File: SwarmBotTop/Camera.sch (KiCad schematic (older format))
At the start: 3 parts, among them J6 Conn_01x24_Female

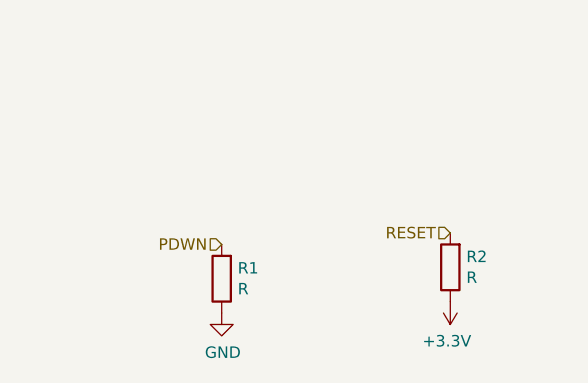
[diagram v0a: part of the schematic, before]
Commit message: Camera routing with all sensors and motors
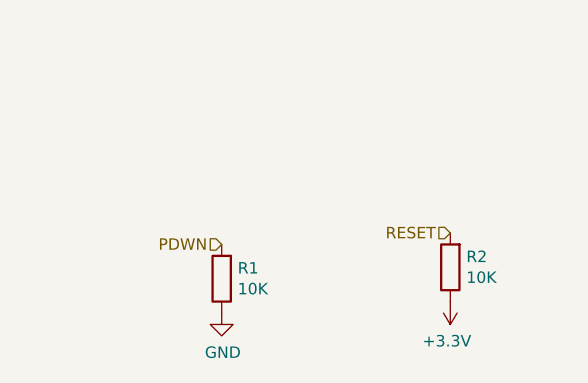
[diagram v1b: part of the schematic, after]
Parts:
- R1, R2: value R -> 10K
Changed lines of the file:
@@
 P 2250 3550
 F 0 "R1" H 2180 3504 50  0000 R CNN
-F 1 "R" H 2180 3595 50  0000 R CNN
+F 1 "10K" H 2180 3595 50  0000 R CNN
 F 2 "Resistor_SMD:R_0402_1005Metric" V 2180 3550 50  0001 C CNN
 F 3 "~" H 2250 3550 50  0001 C CNN
@@
 P 3250 3500
 F 0 "R2" H 3180 3454 50  0000 R CNN
-F 1 "R" H 3180 3545 50  0000 R CNN
+F 1 "10K" H 3180 3545 50  0000 R CNN
 F 2 "Resistor_SMD:R_0402_1005Metric" V 3180 3500 50  0001 C CNN
 F 3 "~" H 3250 3500 50  0001 C CNN

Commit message: V1 ready to order
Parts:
- removed J6: Conn_01x24_Female, Connector_FFC-FPC:Hirose_FH12-24S-0.5SH_1x24-1MP_P0.50mm_Horizontal, symbol Connector:Conn_01x24_Female
- added U9: 62674-241121ALF, ffc:FCI_62674-241121ALF, symbol 62674-241121ALF:62674-241121ALF
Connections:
- net +1V35: now also U9.15
- net +2V8: now also U9.21
- net +3V3: now also U9.14
- net GND: now also U9.10, U9.23
- net HREF: now also U9.16
- net PCKL: now also U9.8
- net PDWN: now also U9.17
- net RESET: now also U9.19
- net SCL: now also U9.20
- net SDA: now also U9.22
- net VSYNC: now also U9.18
- net XCLK: now also U9.12
- net Y2: now also U9.6
- net Y3: now also U9.4
- net Y4: now also U9.3
- net Y5: now also U9.5
- net Y6: now also U9.7
- net Y7: now also U9.9
- net Y8: now also U9.11
- net Y9: now also U9.13
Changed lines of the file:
@@
 $EndDescr
-$Comp
-L Connector:Conn_01x24_Female J6
-U 1 1 5DE89F78
-P 2550 1250
-F 0 "J6" V 2715 1180 50  0000 C CNN
-F 1 "Conn_01x24_Female" V 2624 1180 50  0000 C CNN
-F 2 "Connector_FFC-FPC:Hirose_FH12-24S-0.5SH_1x24-1MP_P0.50mm_Horizontal" H 2550 1250 50  0001 C CNN
-F 3 "~" H 2550 1250 50  0001 C CNN
-	1    2550 1250
-	0    -1   -1   0
-$EndComp
-NoConn ~ 3750 1450
-NoConn ~ 3650 1450
-NoConn ~ 1450 1450
-$Comp
-L power:GND #PWR0167
-U 1 1 5DE8C289
-P 2850 1450
-F 0 "#PWR0167" H 2850 1200 50  0001 C CNN
-F 1 "GND" H 2855 1277 50  0000 C CNN
-F 2 "" H 2850 1450 50  0001 C CNN
-F 3 "" H 2850 1450 50  0001 C CNN
-	1    2850 1450
-	1    0    0    -1
-$EndComp
-$Comp
-L power:GND #PWR0169
-U 1 1 5DE8C618
-P 1550 1450
-F 0 "#PWR0169" H 1550 1200 50  0001 C CNN
-F 1 "GND" H 1555 1277 50  0000 C CNN
-F 2 "" H 1550 1450 50  0001 C CNN
-F 3 "" H 1550 1450 50  0001 C CNN
-	1    1550 1450
-	1    0    0    -1
-$EndComp
-$Comp
-L power:+2V8 #PWR0170
-U 1 1 5DE8CB15
-P 1750 1450
-F 0 "#PWR0170" H 1750 1300 50  0001 C CNN
-F 1 "+2V8" H 1765 1623 50  0000 C CNN
-F 2 "" H 1750 1450 50  0001 C CNN
-F 3 "" H 1750 1450 50  0001 C CNN
-	1    1750 1450
-	-1   0    0    1
-$EndComp
-Text HLabel 1650 1450 3    50   Input ~ 0
-SDA
-Text HLabel 1850 1450 3    50   Input ~ 0
-SCL
-Text HLabel 1950 1450 3    50   Input ~ 0
-RESET
-Text HLabel 2050 1450 3    50   Input ~ 0
-VSYNC
-Text HLabel 2150 1450 3    50   Input ~ 0
-PDWN
-Text HLabel 2250 1450 3    50   Input ~ 0
-HREF
-$Comp
-L power:+1V35 #PWR0171
-U 1 1 5DE8D87F
-P 2350 1450
-F 0 "#PWR0171" H 2350 1300 50  0001 C CNN
-F 1 "+1V35" H 2365 1623 50  0000 C CNN
-F 2 "" H 2350 1450 50  0001 C CNN
-F 3 "" H 2350 1450 50  0001 C CNN
-	1    2350 1450
-	-1   0    0    1
-$EndComp
-$Comp
-L power:+3.3V #PWR0172
-U 1 1 5DE8DDE0
-P 2450 1450
-F 0 "#PWR0172" H 2450 1300 50  0001 C CNN
-F 1 "+3.3V" H 2465 1623 50  0000 C CNN
-F 2 "" H 2450 1450 50  0001 C CNN
-F 3 "" H 2450 1450 50  0001 C CNN
-	1    2450 1450
-	-1   0    0    1
-$EndComp
-Text HLabel 2550 1450 3    50   Input ~ 0
-Y9
-Text HLabel 2650 1450 3    50   Input ~ 0
-XCLK
-Text HLabel 2750 1450 3    50   Input ~ 0
-Y8
-Text HLabel 2950 1450 3    50   Input ~ 0
-Y7
-Text HLabel 3050 1450 3    50   Input ~ 0
-PCKL
-Text HLabel 3150 1450 3    50   Input ~ 0
-Y6
-Text HLabel 3350 1450 3    50   Input ~ 0
-Y5
-Text HLabel 3250 1450 3    50   Input ~ 0
-Y2
-Text HLabel 3450 1450 3    50   Input ~ 0
-Y3
-Text HLabel 3550 1450 3    50   Input ~ 0
-Y4
 $Comp
 L Device:R R1
@@
 	-1   0    0    1
 $EndComp
+NoConn ~ 5000 2350
+NoConn ~ 6100 950
+$Comp
+L power:GND #PWR0167
+U 1 1 5DFE7493
+P 5400 950
+F 0 "#PWR0167" H 5400 700 50  0001 C CNN
+F 1 "GND" H 5405 777 50  0000 C CNN
+F 2 "" H 5400 950 50  0001 C CNN
+F 3 "" H 5400 950 50  0001 C CNN
+	1    5400 950
+	-1   0    0    1
+$EndComp
+Text HLabel 5700 950  1    50   Input ~ 0
+HREF
+$Comp
+L power:+1V35 #PWR0169
+U 1 1 5DFE749A
+P 5700 2350
+F 0 "#PWR0169" H 5700 2200 50  0001 C CNN
+F 1 "+1V35" H 5715 2523 50  0000 C CNN
+F 2 "" H 5700 2350 50  0001 C CNN
+F 3 "" H 5700 2350 50  0001 C CNN
+	1    5700 2350
+	-1   0    0    1
+$EndComp
+$Comp
+L power:+3.3V #PWR0170
+U 1 1 5DFE74A0
+P 5600 950
+F 0 "#PWR0170" H 5600 800 50  0001 C CNN
+F 1 "+3.3V" H 5615 1123 50  0000 C CNN
+F 2 "" H 5600 950 50  0001 C CNN
+F 3 "" H 5600 950 50  0001 C CNN
+	1    5600 950
+	1    0    0    -1
+$EndComp
+Text HLabel 5600 2350 3    50   Input ~ 0
+Y9
+Text HLabel 5500 950  1    50   Input ~ 0
+XCLK
+Text HLabel 5500 2350 3    50   Input ~ 0
+Y8
+Text HLabel 5800 2350 3    50   Input ~ 0
+PDWN
+Text HLabel 5800 950  1    50   Input ~ 0
+VSYNC
+Text HLabel 5900 2350 3    50   Input ~ 0
+RESET
+Text HLabel 5900 950  1    50   Input ~ 0
+SCL
+$Comp
+L power:+2V8 #PWR0171
+U 1 1 5DFE74B9
+P 6000 2350
+F 0 "#PWR0171" H 6000 2200 50  0001 C CNN
+F 1 "+2V8" H 6015 2523 50  0000 C CNN
+F 2 "" H 6000 2350 50  0001 C CNN
+F 3 "" H 6000 2350 50  0001 C CNN
+	1    6000 2350
+	-1   0    0    1
+$EndComp
+Text HLabel 6000 950  1    50   Input ~ 0
+SDA
+$Comp
+L power:GND #PWR0172
+U 1 1 5DFE74C0
+P 6100 2350
+F 0 "#PWR0172" H 6100 2100 50  0001 C CNN
+F 1 "GND" H 6105 2177 50  0000 C CNN
+F 2 "" H 6100 2350 50  0001 C CNN
+F 3 "" H 6100 2350 50  0001 C CNN
+	1    6100 2350
+	1    0    0    -1
+$EndComp
+Text HLabel 5400 2350 3    50   Input ~ 0
+Y7
+Text HLabel 5300 950  1    50   Input ~ 0
+PCKL
+Text HLabel 5300 2350 3    50   Input ~ 0
+Y6
+Text HLabel 5200 950  1    50   Input ~ 0
+Y2
+Text HLabel 5200 2350 3    50   Input ~ 0
+Y5
+Text HLabel 5100 950  1    50   Input ~ 0
+Y3
+Text HLabel 5100 2350 3    50   Input ~ 0
+Y4
+$Comp
+L 62674-241121ALF:62674-241121ALF U9
+U 1 1 5DFB2785
+P 5400 1650
+F 0 "U9" V 5446 717 50  0000 R CNN
+F 1 "62674-241121ALF" V 5355 717 50  0000 R CNN
+F 2 "ffc:FCI_62674-241121ALF" H 5400 1650 50  0001 L BNN
+F 3 "62674-241121ALF" H 5400 1650 50  0001 L BNN
+F 4 "03M2162" H 5400 1650 50  0001 L BNN "Field4"
+F 5 "1830630" H 5400 1650 50  0001 L BNN "Field5"
+F 6 "FCI" H 5400 1650 50  0001 L BNN "Field6"
+F 7 "CONN-24POS" H 5400 1650 50  0001 L BNN "Field7"
+	1    5400 1650
+	0    -1   -1   0
+$EndComp
+NoConn ~ 5000 950
 $EndSCHEMATC
